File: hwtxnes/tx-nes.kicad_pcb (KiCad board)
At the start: 2 copper layers, 78.9 x 22.1 mm, 27 parts, among them IC1 ATMEGA328-A, J1 POWER_JACK, P1 nRF, P2 ISP, P3 DIL16, P7 RX, P8 TX, SW1 DPDT, U1 TCR2EF, U2 MCP73832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

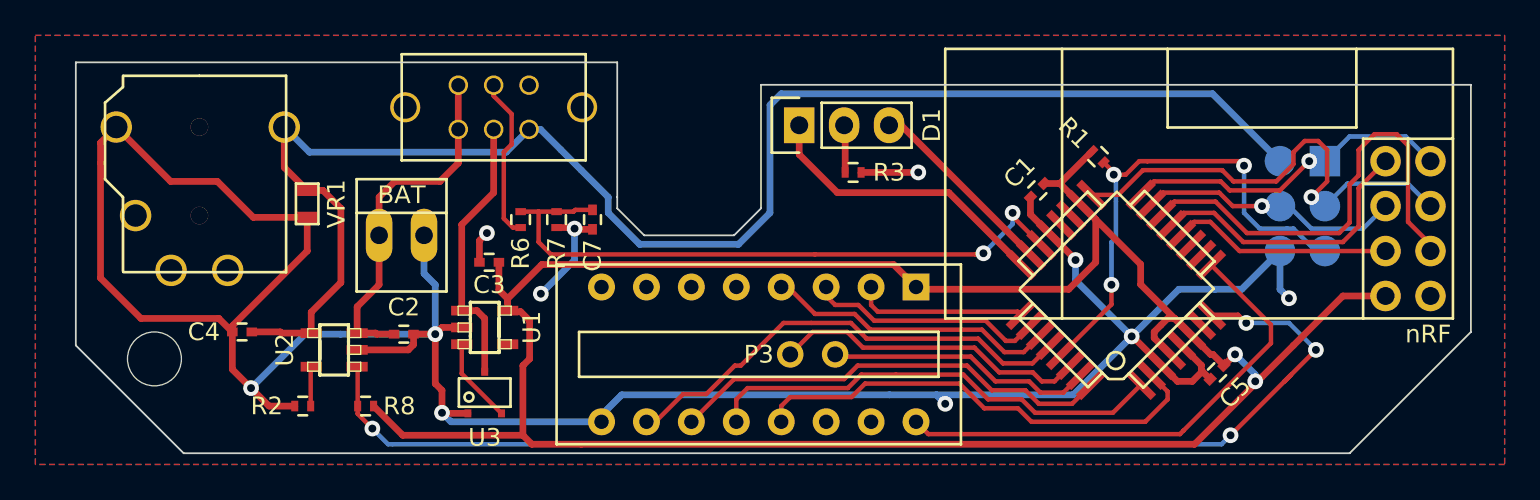
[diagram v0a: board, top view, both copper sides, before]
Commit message: Holes big enough to fit standard pins.
The 16 pin interconnect going to the main board has holes that don't
really fit a standard 0.1" header pin.  They fit, only barely with too
much force.  The new size matches the TX/RX holes, which fit the pin
comfortably.
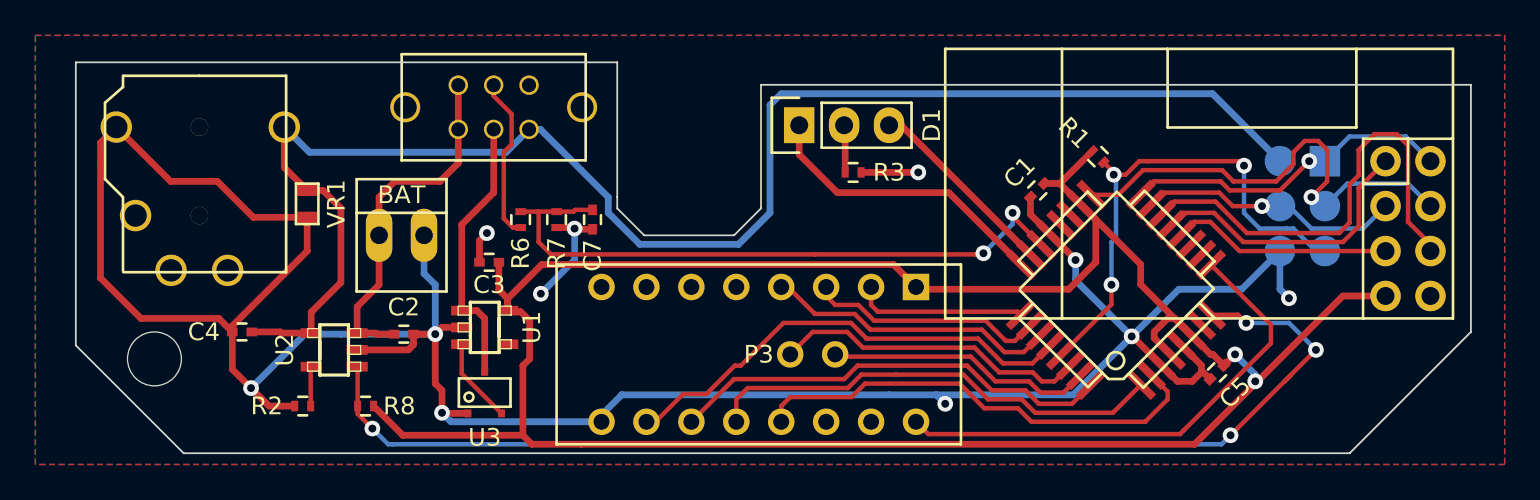
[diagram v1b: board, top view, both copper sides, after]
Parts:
- P1: footprint nRF_Header_2x04 -> nesRF TX:nRF_Header_2x04
- P3: footprint Discret:SWDIP8 -> nesRF TX:NES_PCB_INTERCONNECT
- SW1: footprint SK22D01 -> nesRF TX:SK22D01

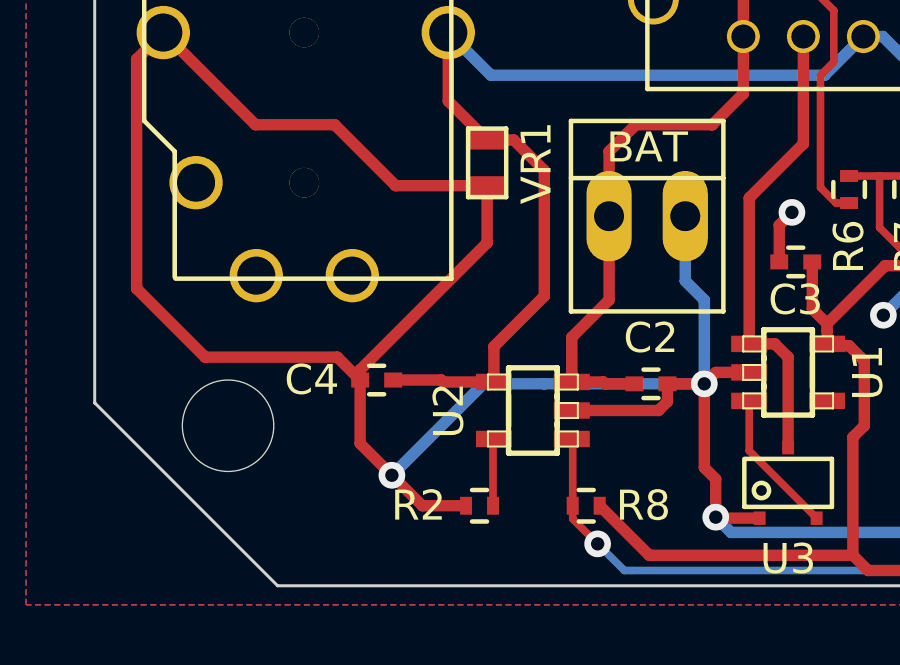
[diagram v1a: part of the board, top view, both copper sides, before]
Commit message: Move mounting hole to actual standoff position.
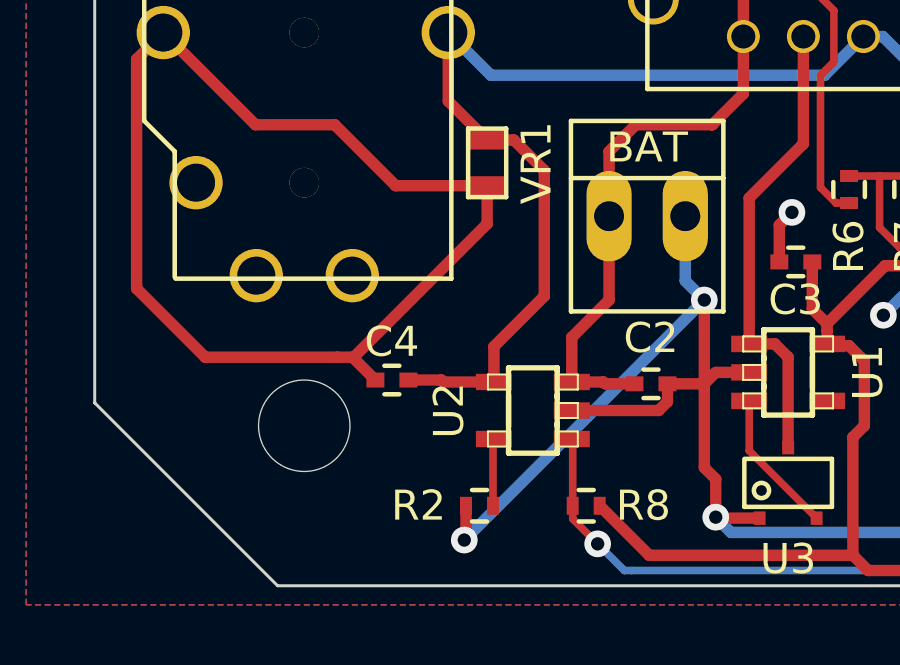
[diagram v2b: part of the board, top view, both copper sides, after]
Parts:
- moved Mount_Hole 2.54 mm to (54.4, 40.6)
- moved C4 0.51 mm to (57.3, 39.1)
- renumbered REF** to Mount_Hole
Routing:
- net GND: track 161.0 -> 155.1 mm
- net +5V: track 86.9 -> 86.4 mm
